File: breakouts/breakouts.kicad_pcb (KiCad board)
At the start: 2 copper layers, 3 parts, among them IC1 SN74AVCH16T245VR, J1 Conn_01x24_Male, J2 Conn_01x24_Male

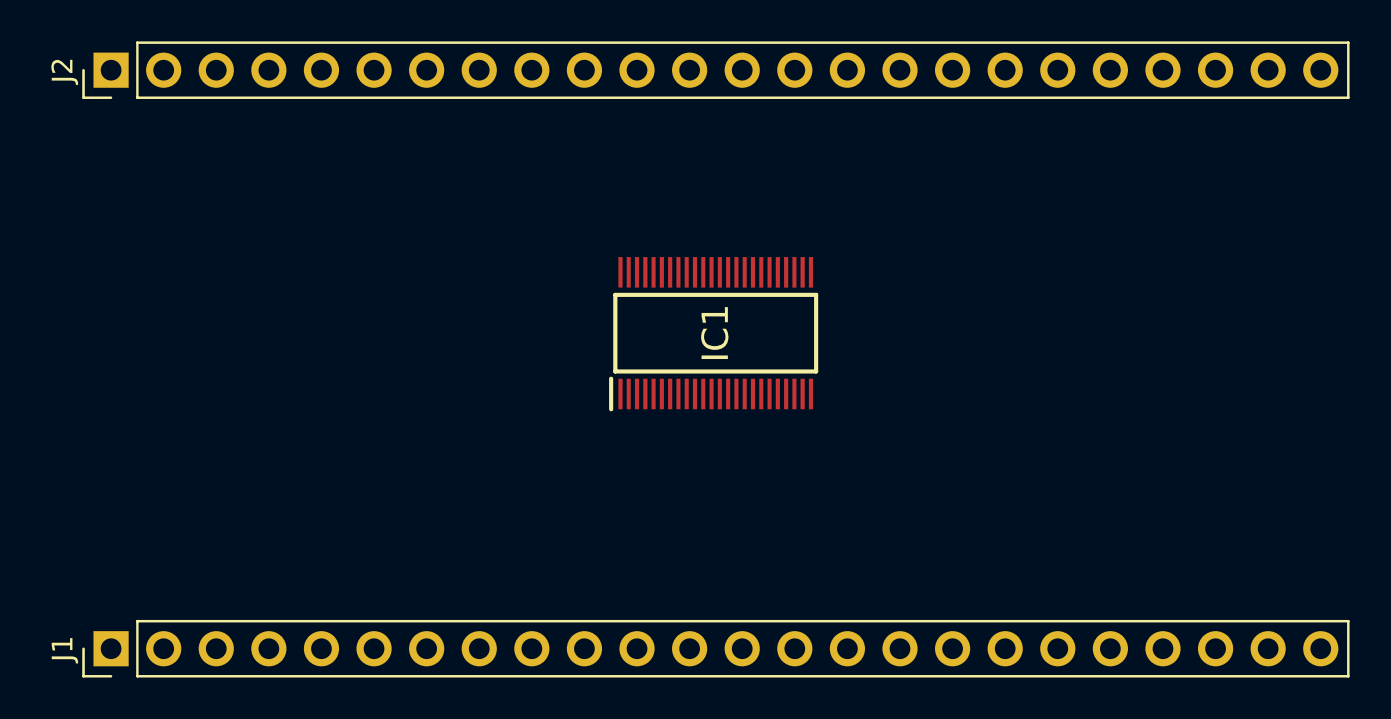
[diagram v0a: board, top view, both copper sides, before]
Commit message: Putting traces on level shift breakout
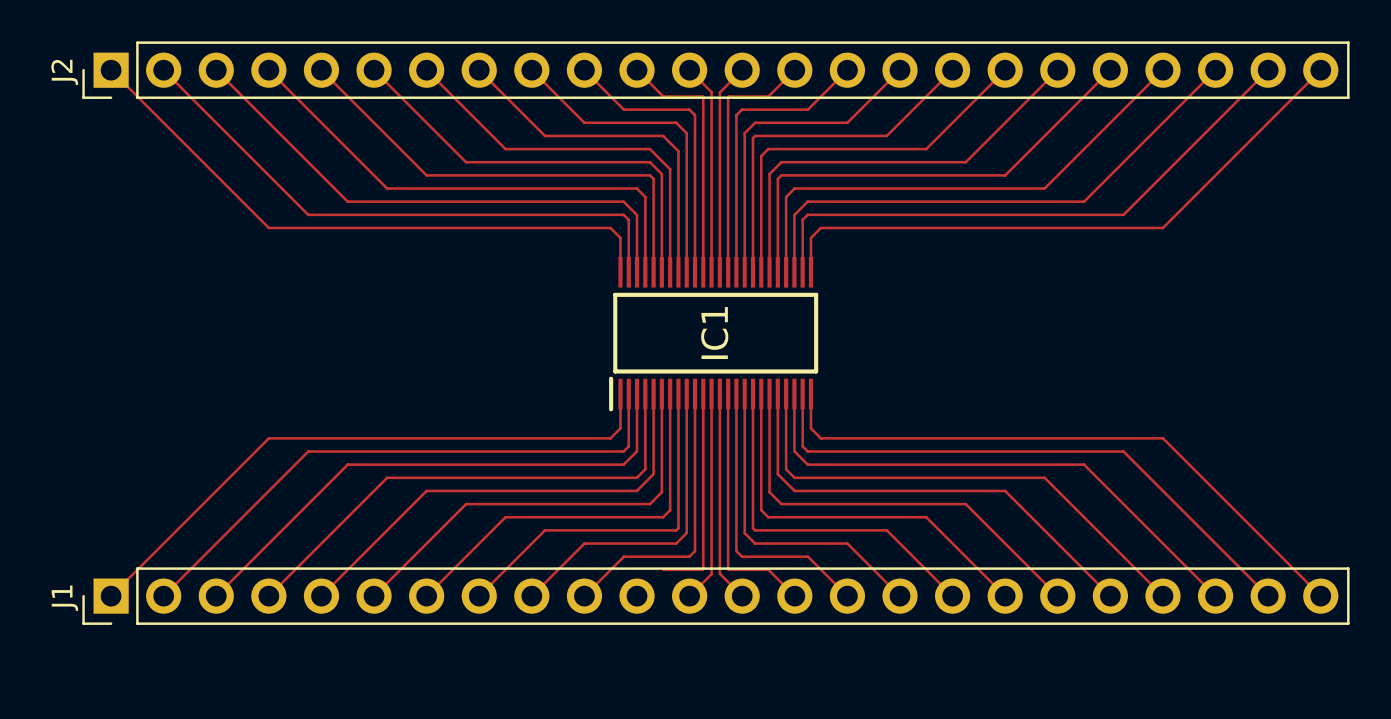
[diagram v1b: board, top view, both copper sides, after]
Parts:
- moved J1 2.54 mm to (123.2, 114.3)
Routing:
- net Net-(IC1-Pad25): track 0.00 -> 29.6 mm
- net Net-(IC1-Pad24): track 0.00 -> 29.6 mm
- net Net-(IC1-Pad48): track 0.00 -> 29.6 mm
- net Net-(IC1-Pad1): track 0.00 -> 29.6 mm
- net Net-(IC1-Pad26): track 0.00 -> 28.0 mm
- net Net-(IC1-Pad23): track 0.00 -> 28.0 mm
- net Net-(IC1-Pad47): track 0.00 -> 28.0 mm
- net Net-(IC1-Pad2): track 0.00 -> 28.0 mm
- net Net-(IC1-Pad27): track 0.00 -> 26.0 mm
- net Net-(IC1-Pad22): track 0.00 -> 26.0 mm
- net Net-(IC1-Pad46): track 0.00 -> 26.0 mm
- net Net-(IC1-Pad3): track 0.00 -> 26.0 mm
- net Net-(IC1-Pad21): track 0.00 -> 24.4 mm
- net Net-(IC1-Pad28): track 0.00 -> 24.4 mm
- net Net-(IC1-Pad4): track 0.00 -> 24.4 mm
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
